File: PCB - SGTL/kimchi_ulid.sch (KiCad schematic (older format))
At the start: 43 parts, among them J1 RCJ-2123, J2 DF40HC(3.5)-60DS, J3 DF40HC(3.5)-60DS, J4 RCJ-2123, J5 54-00176, U1 24C32, U2 SGTL5000XNLA3

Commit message: SGTL Version
 SGTL version finished, need feedback, chip is weird the route is too
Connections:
- wire segments 162 -> 160
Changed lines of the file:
@@
 Wire Wire Line
 	14300 7700 14300 7550
-Wire Wire Line
-	2200 9400 1200 9400
 $Comp
 L kimchi_ulid:T491D227M010AT C10
@@
 Text GLabel 4700 6650 0    50   Input ~ 0
 SAI3_TXFS
-Text GLabel 5200 7150 0    50   Input ~ 0
+Text GLabel 7550 6950 2    50   Input ~ 0
 SAI3_RXD
-Text GLabel 5200 7250 0    50   Input ~ 0
-SAI3_RXFS
 Text GLabel 5200 7050 0    50   Input ~ 0
 SAI3_TXD
@@
 Wire Wire Line
 	6050 7050 5200 7050
-Text GLabel 1900 9600 0    50   Input ~ 0
-I2C3_SDA
-Text GLabel 1900 9500 0    50   Input ~ 0
-I2C3_SCL
-Wire Wire Line
-	1900 9500 2200 9500
-Wire Wire Line
-	2200 9600 1900 9600
 $Comp
 L kimchi_ulid:GG_LOGO L1
@@
 	5000 7900 3850 7900
 Connection ~ 5000 7900
+Text GLabel 5200 7150 0    50   Input ~ 0
+I2C3_SDA
+Text GLabel 5200 7250 0    50   Input ~ 0
+I2C3_SCL
+Wire Wire Line
+	7450 6950 7550 6950
 $EndSCHEMATC

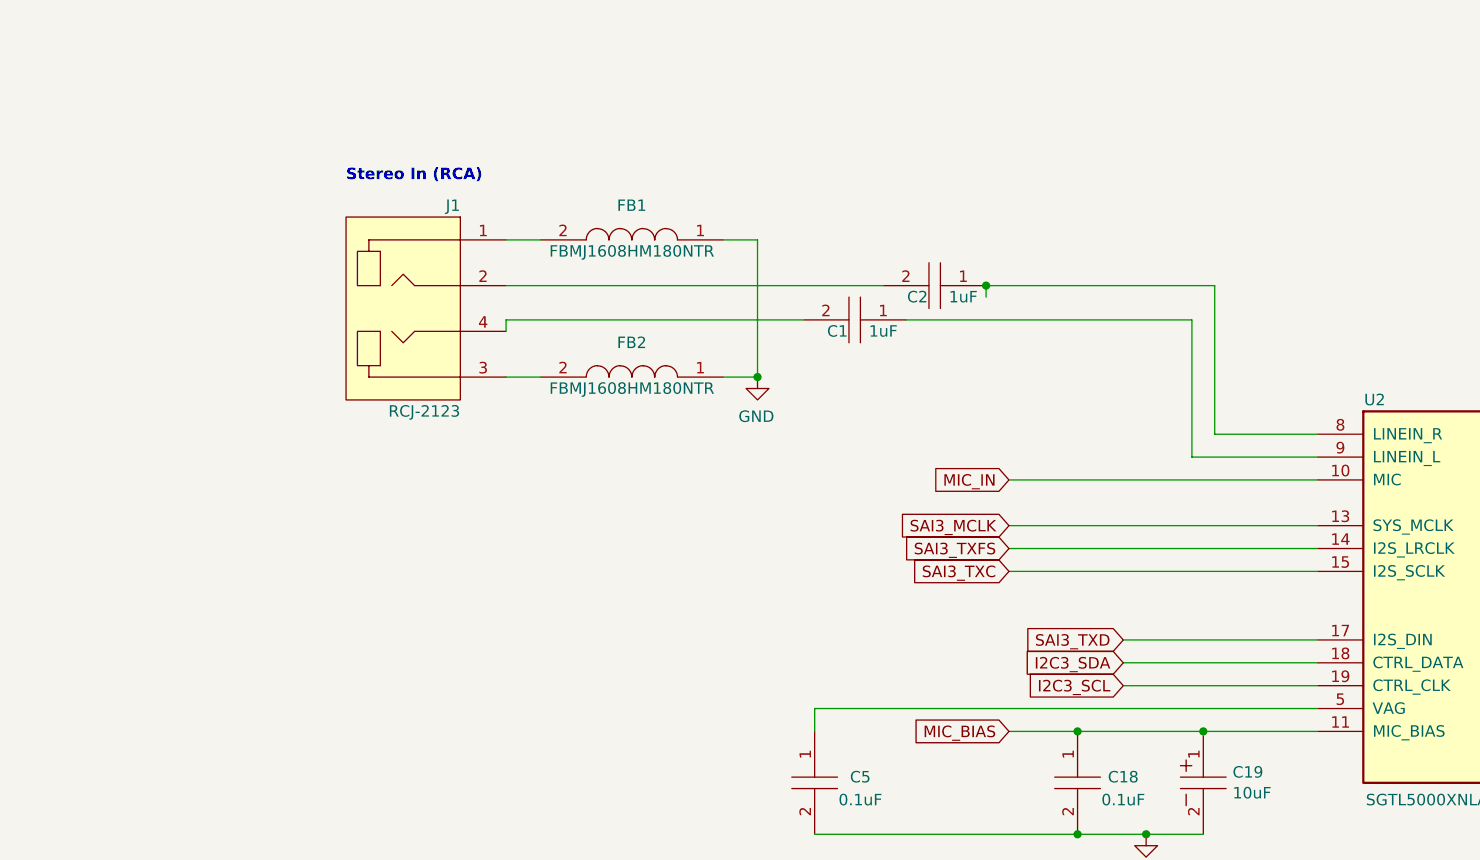
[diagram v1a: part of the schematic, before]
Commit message: Test Points
Test points added, also traces cleaned up and widened in places where more current capacity is required or appreciated.
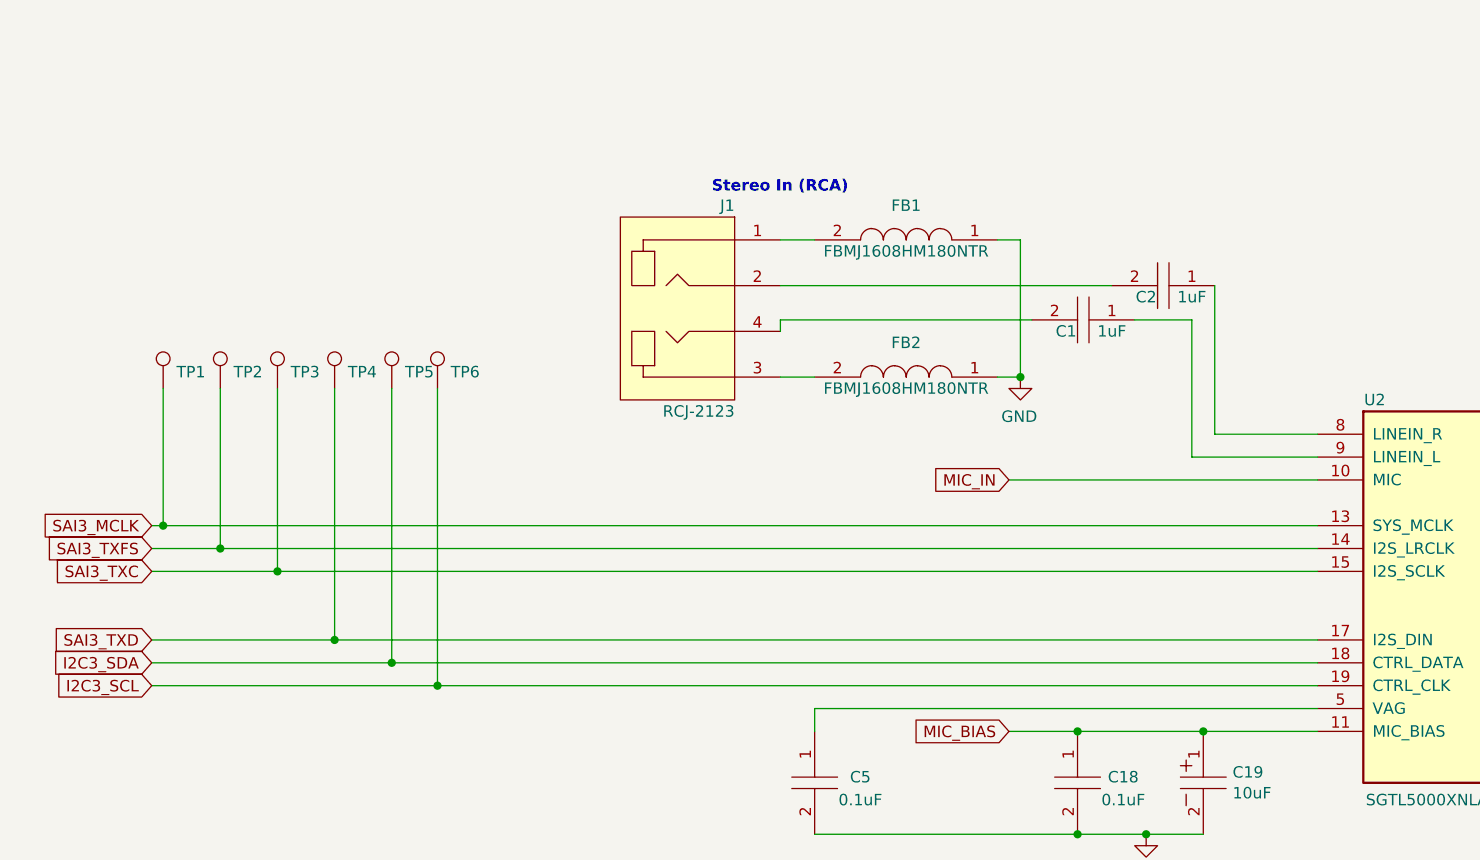
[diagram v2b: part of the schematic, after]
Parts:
- added TP1, TP2, TP3, TP4, TP5, TP6: TestPoint, kimchi_ulid:TestPoint_Pad_D1.0mm, symbol kimchi_ulid:TestPoint
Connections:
- net I2C3_SCL: now also TP6.1
- net I2C3_SDA: now also TP5.1
- net SAI3_MCLK: now also TP1.1
- net SAI3_TXC: now also TP3.1
- net SAI3_TXD: now also TP4.1
- net SAI3_TXFS: now also TP2.1
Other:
- moved on the sheet: C1, C2, FB1, FB2, J1

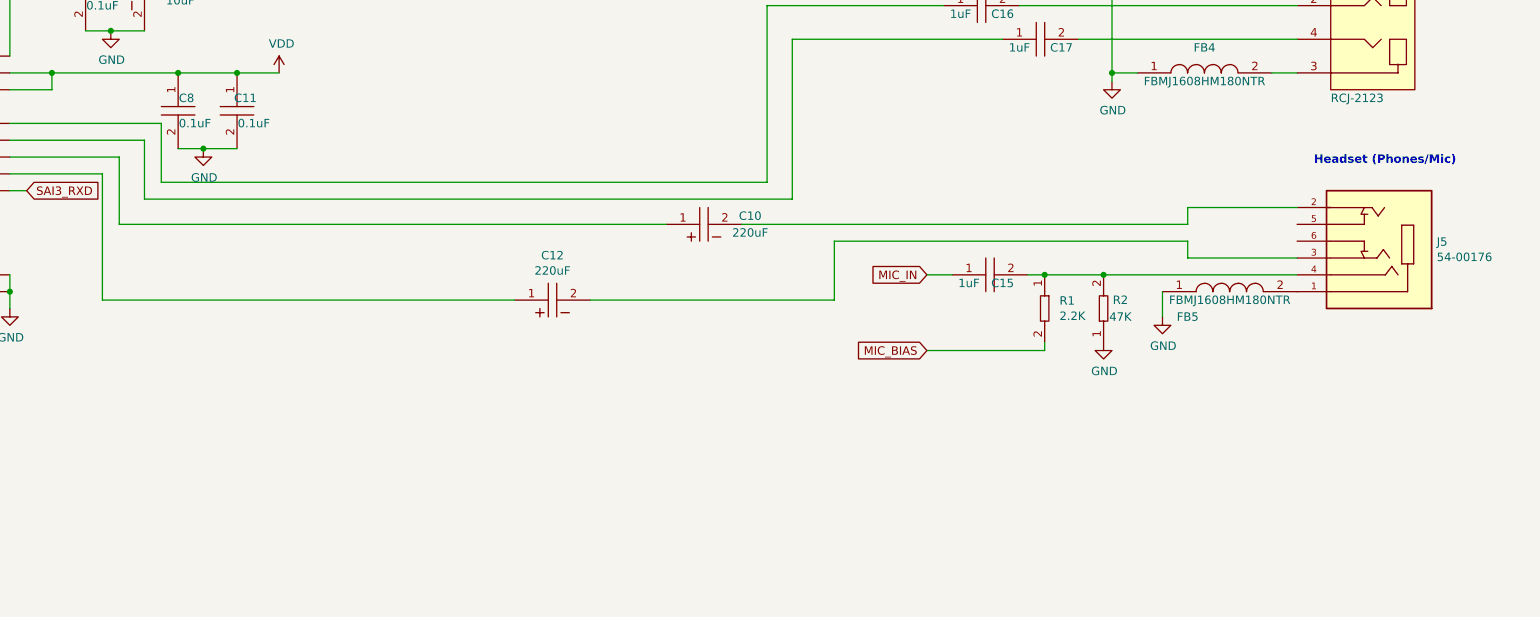
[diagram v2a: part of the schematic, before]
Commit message: Headphone Detect and DRC
Cleared DRC violations, added and implemented a headphone detect circuit.
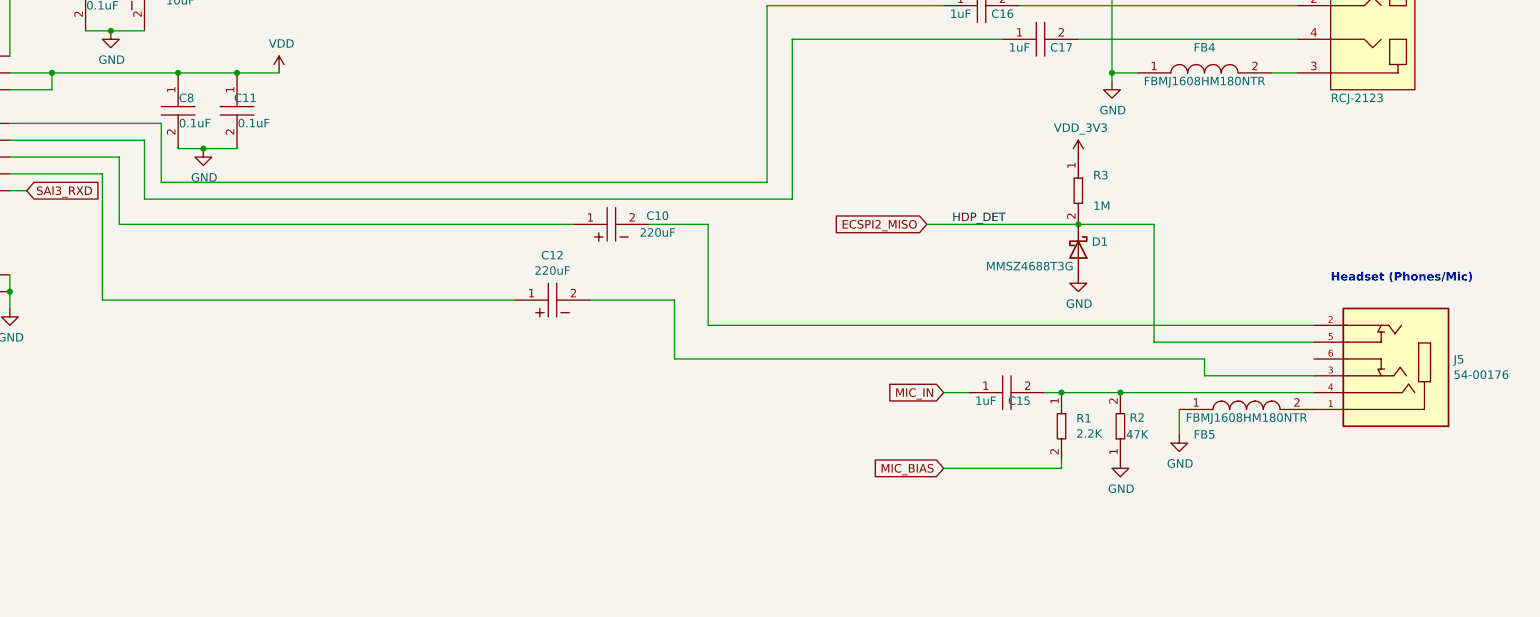
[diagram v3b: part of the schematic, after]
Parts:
- added D1: MMSZ4688T3G, kimchi_ulid:MMSZ4688T3G, symbol kimchi_ulid:MMSZ4688T3G
- added R3: AC0402FR-071ML, kimchi_ulid:R0402, symbol kimchi_ulid:AC0402FR-071ML
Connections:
- net ECSPI2_MISO: now also J5.5, D1.1 (K), R3.2
- net GND: now also D1.2 (A)
- net VDD_3V3: now also R3.1
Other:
- moved on the sheet: C10, C15, FB5, J5, R1, R2
